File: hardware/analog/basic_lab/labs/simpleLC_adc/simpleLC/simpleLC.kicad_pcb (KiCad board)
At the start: 2 copper layers, 77 x 27.9 mm, 10 parts, among them J1 Conn_01x04_Male, Q1 FQP27P06, Q2 BC547

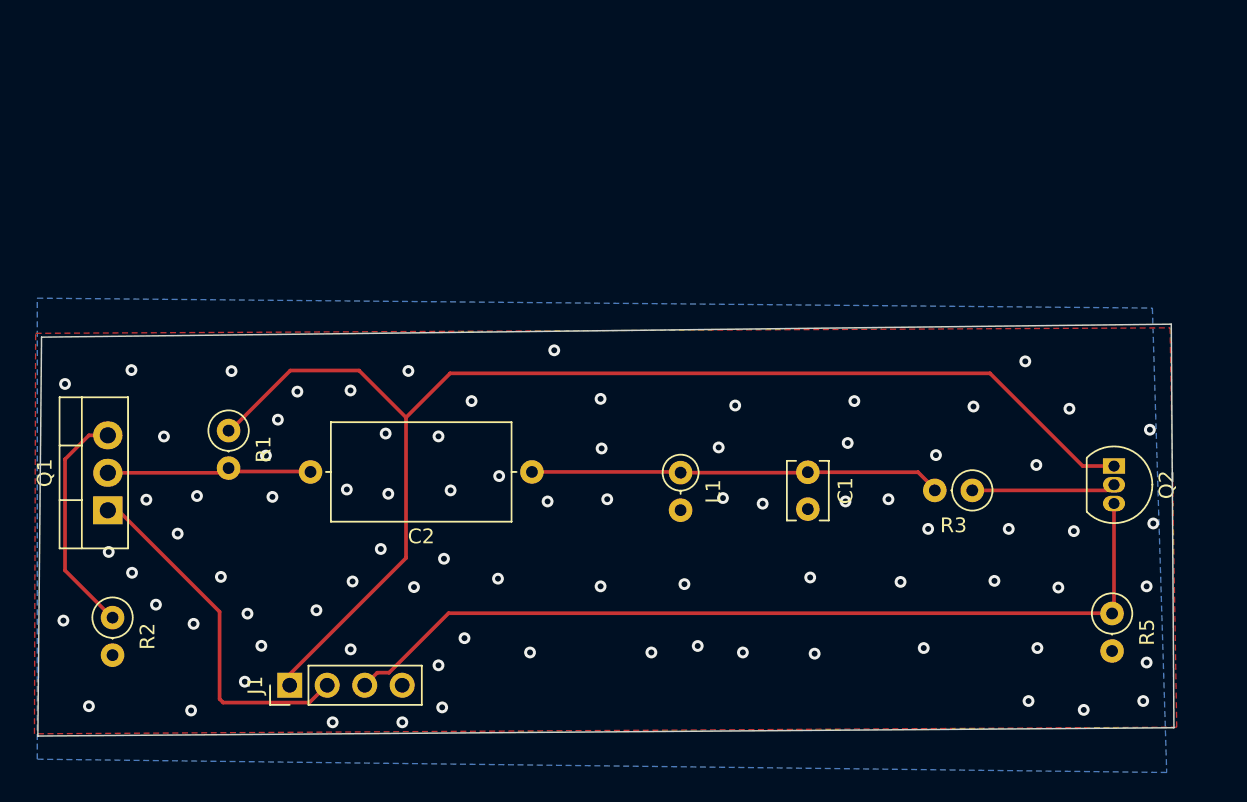
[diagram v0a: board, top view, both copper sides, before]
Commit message: Simple lc => adc v1, jlcpcb order
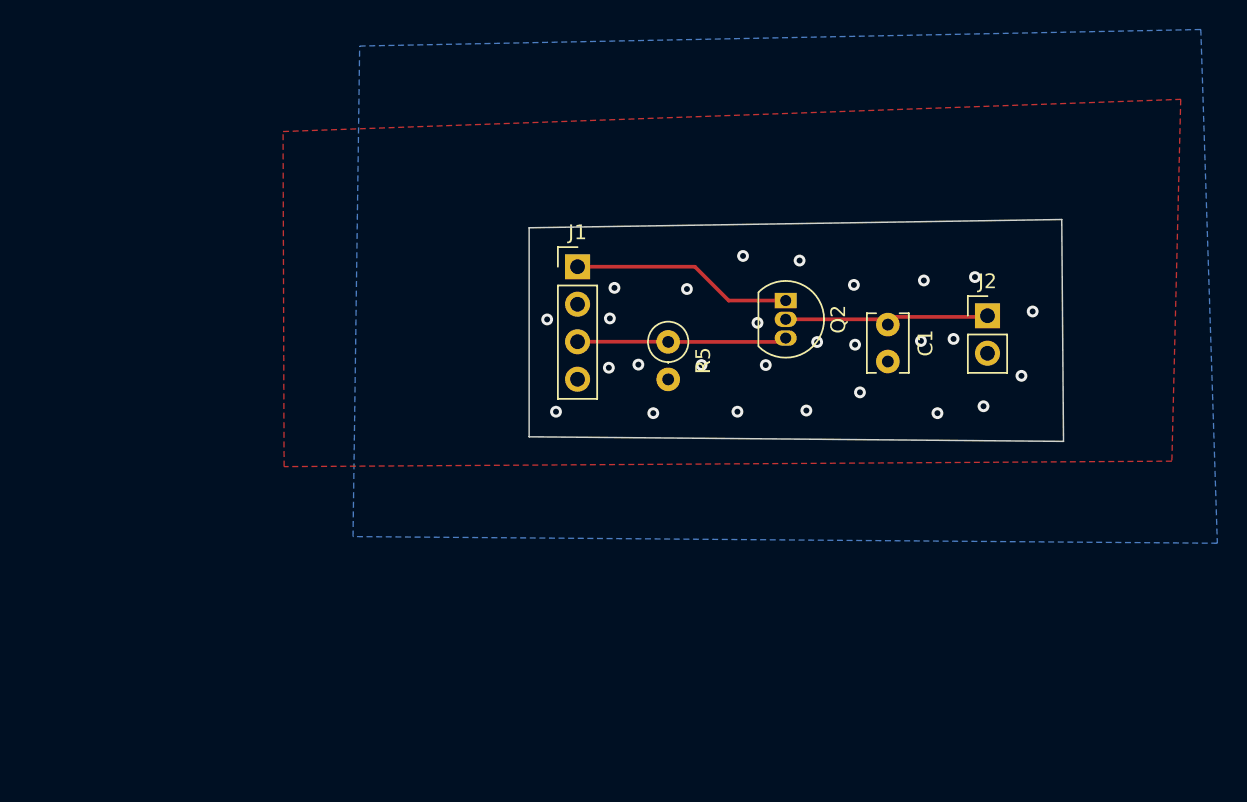
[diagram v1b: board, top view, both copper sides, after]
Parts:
- removed C2: C, Capacitor_THT:C_Axial_L12.0mm_D6.5mm_P15.00mm_Horizontal
- removed L1: L, Inductor_THT:L_Axial_L5.3mm_D2.2mm_P2.54mm_Vertical_Vishay_IM-1
- removed Q1: FQP27P06, Package_TO_SOT_THT:TO-220-3_Vertical
- removed R1, R2, R3: R, Resistor_THT:R_Axial_DIN0207_L6.3mm_D2.5mm_P2.54mm_Vertical
- added J2: Conn_01x02_Male, Connector_PinHeader_2.54mm:PinHeader_1x02_P2.54mm_Vertical, F.Cu at (194.7, 93.0)
- moved R5 35.3 mm to (173.1, 94.8)
- moved J1 34.4 mm to (166.9, 89.7), turned to 0 degrees
- moved Q2 24.9 mm to (181.0, 92.0)
- moved C1 11.4 mm to (187.9, 93.6)
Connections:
- J1 pad 2: din -> Net-(J1-Pad2)
- Q2 pad 2: Net-(Q2-Pad2) -> Net-(C1-Pad1)
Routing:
- net +3V3: track 88.4 -> 15.0 mm
- net aout: track 60.1 -> 14.2 mm
- net din: track 24.2 -> 0.00 mm
- net Net-(Q1-Pad3): track 15.7 -> 0.00 mm
- net Net-(C1-Pad1): track 27.9 -> 14.0 mm
- net Net-(C2-Pad2): track 13.8 -> 0.00 mm
- net Net-(Q2-Pad2): track 9.60 -> 0.00 mm
- net GND: vias 84 -> 27
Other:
- board size 77 x 27.9 mm -> 36.2 x 15 mm

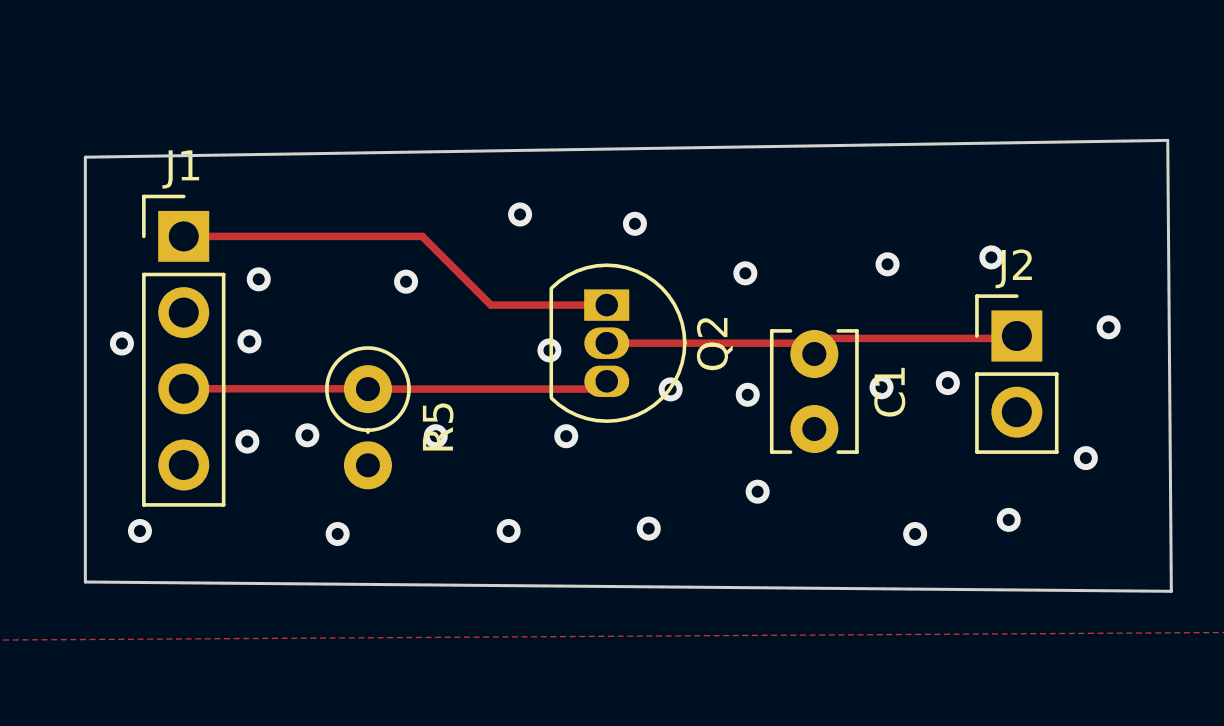
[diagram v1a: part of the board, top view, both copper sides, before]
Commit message: pwm => adc: XFRM amplifier PCB
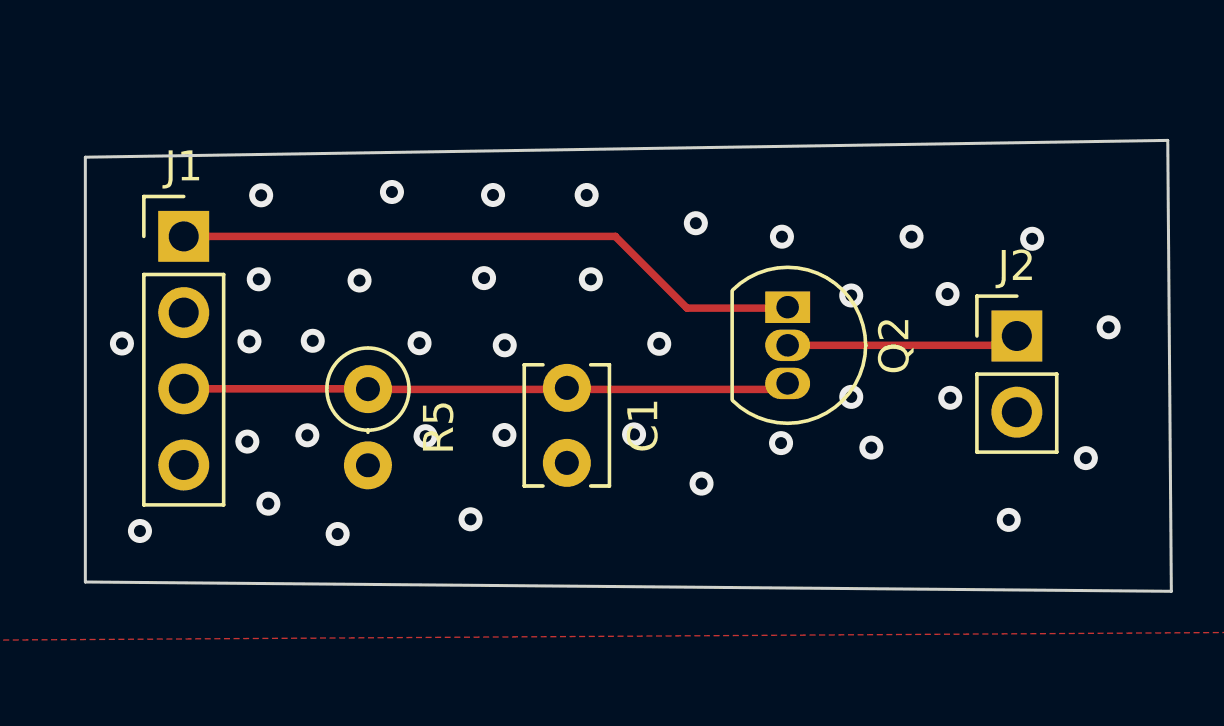
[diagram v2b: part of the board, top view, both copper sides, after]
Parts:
- moved C1 8.33 mm to (179.7, 94.7)
- moved Q2 6.03 mm to (187.0, 92.0)
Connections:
- C1 pad 1: Net-(C1-Pad1) -> aout
- J2 pad 1: Net-(C1-Pad1) -> Net-(J2-Pad1)
- Q2 pad 2: Net-(C1-Pad1) -> Net-(J2-Pad1)
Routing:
- net Net-(C1-Pad1): track 14.0 -> 0.00 mm
- net Net-(J2-Pad1): track 0.00 -> 7.84 mm
- net +3V3: track 15.0 -> 21.2 mm
- net aout: track 14.2 -> 20.2 mm
- net GND: vias 27 -> 37

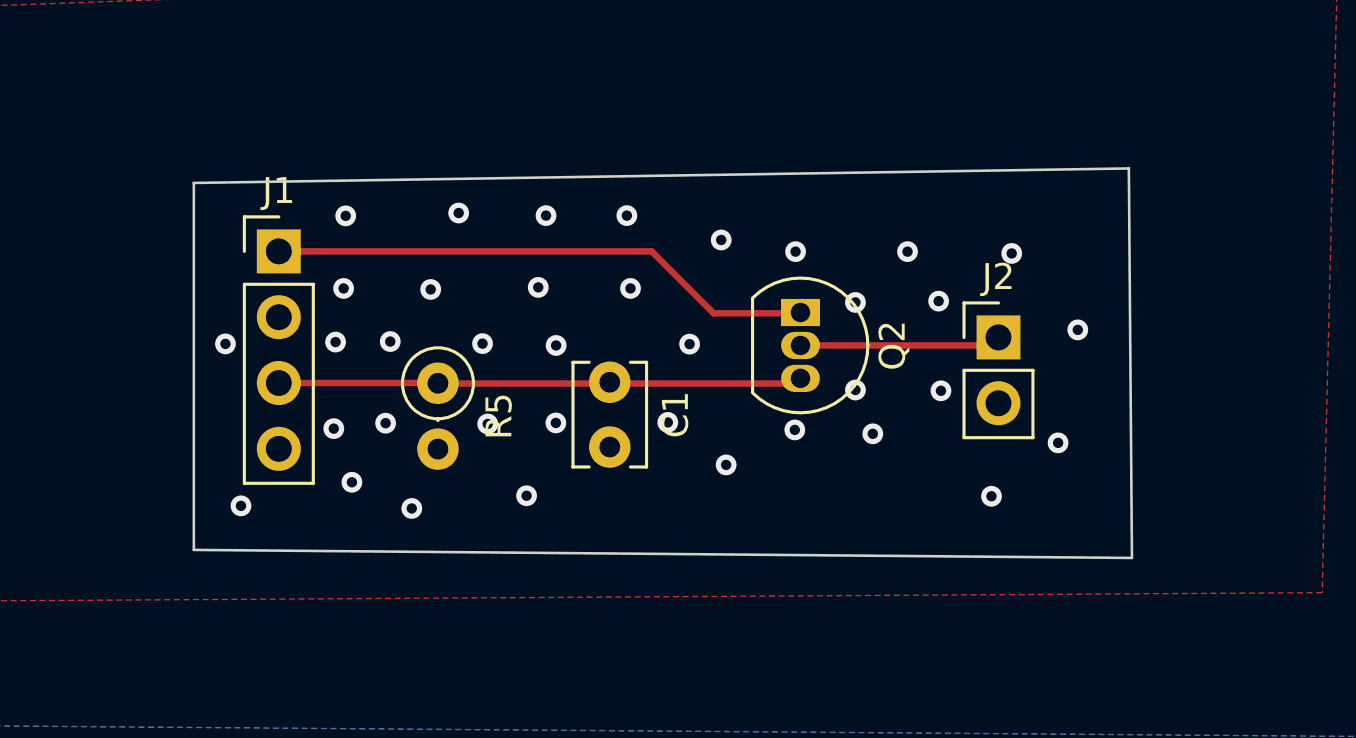
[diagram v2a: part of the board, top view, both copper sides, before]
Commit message: pwm => adc: XFRM amplifier PCB
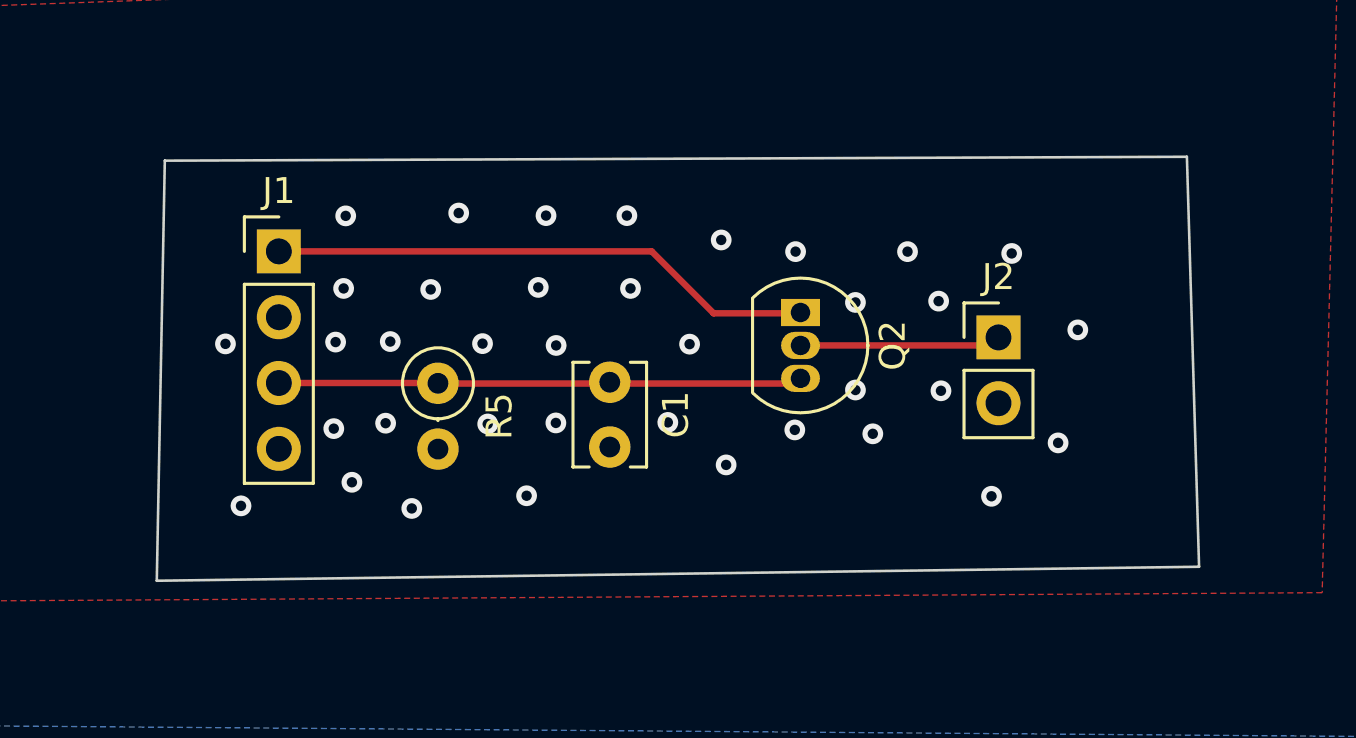
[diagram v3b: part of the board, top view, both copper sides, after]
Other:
- board size 36.2 x 15 mm -> 40.2 x 16.4 mm
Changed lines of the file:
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@@
     (add_net aout)
+  )
+  (module Connector_PinHeader_2.54mm:PinHeader_1x04_P2.54mm_Vertical (layer F.Cu)
+    (at 166.91 89.68)
+    (descr "Through hole straight pin header, 1x04, 2.54mm pitch, single row")
+    (tags "Through hole pin header THT 1x04 2.54mm single row")
+    (fp_text reference J1 (at 0 -2.33) (layer F.SilkS)
+      (effects (font (size 1 1) (thickness 0.15)))
+    )
+    (fp_text value Conn_01x04_Male (at 0 9.95) (layer F.Fab)
+      (effects (font (size 1 1) (thickness 0.15)))
+    )
+    (fp_line (start 1.8 -1.8) (end -1.8 -1.8) (layer F.CrtYd) (width 0.05))
+    (fp_line (start 1.8 9.4) (end 1.8 -1.8) (layer F.CrtYd) (width 0.05))
+    (fp_line (start -1.8 9.4) (end 1.8 9.4) (layer F.CrtYd) (width 0.05))
+    (fp_line (start -1.8 -1.8) (end -1.8 9.4) (layer F.CrtYd) (width 0.05))
+    (fp_line (start -1.33 -1.33) (end 0 -1.33) (layer F.SilkS) (width 0.12))
+    (fp_line (start -1.33 0) (end -1.33 -1.33) (layer F.SilkS) (width 0.12))
+    (fp_line (start -1.33 1.27) (end 1.33 1.27) (layer F.SilkS) (width 0.12))
+    (fp_line (start 1.33 1.27) (end 1.33 8.95) (layer F.SilkS) (width 0.12))
+    (fp_line (start -1.33 1.27) (end -1.33 8.95) (layer F.SilkS) (width 0.12))
+    (fp_line (start -1.33 8.95) (end 1.33 8.95) (layer F.SilkS) (width 0.12))
+    (fp_line (start -1.27 -0.635) (end -0.635 -1.27) (layer F.Fab) (width 0.1))
+    (fp_line (start -1.27 8.89) (end -1.27 -0.635) (layer F.Fab) (width 0.1))
+    (fp_line (start 1.27 8.89) (end -1.27 8.89) (layer F.Fab) (width 0.1))
+    (fp_line (start 1.27 -1.27) (end 1.27 8.89) (layer F.Fab) (width 0.1))
+    (fp_line (start -0.635 -1.27) (end 1.27 -1.27) (layer F.Fab) (width 0.1))
+    (fp_text user %R (at 0 3.81 90) (layer F.Fab)
+      (effects (font (size 1 1) (thickness 0.15)))
+    )
+    (pad 4 thru_hole oval (at 0 7.62) (size 1.7 1.7) (drill 1) (layers *.Cu *.Mask)
+      (net 1 GND))
+    (pad 3 thru_hole oval (at 0 5.08) (size 1.7 1.7) (drill 1) (layers *.Cu *.Mask)
+      (net 2 aout))
+    (pad 2 thru_hole oval (at 0 2.54) (size 1.7 1.7) (drill 1) (layers *.Cu *.Mask)
+      (net 4 "Net-(J1-Pad2)"))
+    (pad 1 thru_hole rect (at 0 0) (size 1.7 1.7) (drill 1) (layers *.Cu *.Mask)
+      (net 3 +3V3))
+    (model ${KISYS3DMOD}/Connector_PinHeader_2.54mm.3dshapes/PinHeader_1x04_P2.54mm_Vertical.wrl
+      (at (xyz 0 0 0))
+      (scale (xyz 1 1 1))
+      (rotate (xyz 0 0 0))
+    )
   )
   (module Resistor_THT:R_Axial_DIN0207_L6.3mm_D2.5mm_P2.54mm_Vertical (layer F.Cu)
@@
     )
   )
-  (module Connector_PinHeader_2.54mm:PinHeader_1x04_P2.54mm_Vertical (layer F.Cu)
-    (at 166.91 89.68)
-    (descr "Through hole straight pin header, 1x04, 2.54mm pitch, single row")
-    (tags "Through hole pin header THT 1x04 2.54mm single row")
-    (fp_text reference J1 (at 0 -2.33) (layer F.SilkS)
-      (effects (font (size 1 1) (thickness 0.15)))
-    )
-    (fp_text value Conn_01x04_Male (at 0 9.95) (layer F.Fab)
-      (effects (font (size 1 1) (thickness 0.15)))
-    )
-    (fp_line (start 1.8 -1.8) (end -1.8 -1.8) (layer F.CrtYd) (width 0.05))
-    (fp_line (start 1.8 9.4) (end 1.8 -1.8) (layer F.CrtYd) (width 0.05))
-    (fp_line (start -1.8 9.4) (end 1.8 9.4) (layer F.CrtYd) (width 0.05))
-    (fp_line (start -1.8 -1.8) (end -1.8 9.4) (layer F.CrtYd) (width 0.05))
-    (fp_line (start -1.33 -1.33) (end 0 -1.33) (layer F.SilkS) (width 0.12))
-    (fp_line (start -1.33 0) (end -1.33 -1.33) (layer F.SilkS) (width 0.12))
-    (fp_line (start -1.33 1.27) (end 1.33 1.27) (layer F.SilkS) (width 0.12))
-    (fp_line (start 1.33 1.27) (end 1.33 8.95) (layer F.SilkS) (width 0.12))
-    (fp_line (start -1.33 1.27) (end -1.33 8.95) (layer F.SilkS) (width 0.12))
-    (fp_line (start -1.33 8.95) (end 1.33 8.95) (layer F.SilkS) (width 0.12))
-    (fp_line (start -1.27 -0.635) (end -0.635 -1.27) (layer F.Fab) (width 0.1))
-    (fp_line (start -1.27 8.89) (end -1.27 -0.635) (layer F.Fab) (width 0.1))
-    (fp_line (start 1.27 8.89) (end -1.27 8.89) (layer F.Fab) (width 0.1))
-    (fp_line (start 1.27 -1.27) (end 1.27 8.89) (layer F.Fab) (width 0.1))
-    (fp_line (start -0.635 -1.27) (end 1.27 -1.27) (layer F.Fab) (width 0.1))
-    (fp_text user %R (at 0 3.81 90) (layer F.Fab)
-      (effects (font (size 1 1) (thickness 0.15)))
-    )
-    (pad 4 thru_hole oval (at 0 7.62) (size 1.7 1.7) (drill 1) (layers *.Cu *.Mask)
-      (net 1 GND))
-    (pad 3 thru_hole oval (at 0 5.08) (size 1.7 1.7) (drill 1) (layers *.Cu *.Mask)
-      (net 2 aout))
-    (pad 2 thru_hole oval (at 0 2.54) (size 1.7 1.7) (drill 1) (layers *.Cu *.Mask)
-      (net 4 "Net-(J1-Pad2)"))
-    (pad 1 thru_hole rect (at 0 0) (size 1.7 1.7) (drill 1) (layers *.Cu *.Mask)
-      (net 3 +3V3))
-    (model ${KISYS3DMOD}/Connector_PinHeader_2.54mm.3dshapes/PinHeader_1x04_P2.54mm_Vertical.wrl
-      (at (xyz 0 0 0))
-      (scale (xyz 1 1 1))
-      (rotate (xyz 0 0 0))
-    )
-  )
   (module Capacitor_THT:C_Disc_D3.8mm_W2.6mm_P2.50mm (layer F.Cu)
     (at 179.68 94.73 270)
@@
     )
   )
-  (gr_line (start 199.71 86.48) (end 199.83 101.51) (layer Edge.Cuts) (width 0.1))
-  (gr_line (start 163.63 87.04) (end 199.71 86.48) (layer Edge.Cuts) (width 0.1))
-  (gr_line (start 163.63 101.2) (end 163.63 87.04) (layer Edge.Cuts) (width 0.1))
-  (gr_line (start 199.83 101.51) (end 163.63 101.2) (layer Edge.Cuts) (width 0.1))
+  (gr_line (start 201.95 86.03) (end 202.42 101.85) (layer Edge.Cuts) (width 0.1))
+  (gr_line (start 162.51 86.18) (end 201.95 86.03) (layer Edge.Cuts) (width 0.1))
+  (gr_line (start 162.2 102.39) (end 162.51 86.18) (layer Edge.Cuts) (width 0.1))
+  (gr_line (start 202.42 101.85) (end 162.2 102.39) (layer Edge.Cuts) (width 0.1))
   (via (at 169.41 91.11) (size 0.8) (drill 0.4) (layers F.Cu B.Cu) (net 1))
   (via (at 169.1 93.18) (size 0.8) (drill 0.4) (layers F.Cu B.Cu) (net 1))
